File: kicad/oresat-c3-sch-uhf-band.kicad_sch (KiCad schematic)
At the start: 125 parts, among them Q3 NTR4101, Q4 PMV45EN, U16 AX5043, U18 LT5534, U19 BDCN-20-13+, U20 QPC1022, U21 TQP7M9105, U22 LT5534, U25 SN74LVC1G11IDCKRQ1, U26 TLV7041DBV, U27 LP2985AIM5-1.8_NOPB, U29 TQP3M9036, U32 SF2446E, U33 SF2446E, U40 MAX941EUA+, X1 TYKTBLSANF-16.000000

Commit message: Last of the ERC and DRC errors! only polishing left.
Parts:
- TP901, TP902, TP903, TP904, TP905, TP906, TP907, TP908, TP909: now left out of the parts list
- U40: footprint oresat-c3:21-0036K_MXM -> oresat-ics:LINEAR-MSOP-8-AND-MAXIM-UMAX-8-21-0036
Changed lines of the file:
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@@
   )
   (symbol (lib_id "oresat-misc:Test-Point-RF-Probe-Stripline") (at 281.94 101.6 180) (unit 1)
-    (in_bom yes) (on_board yes) (dnp no)
+    (in_bom no) (on_board yes) (dnp no)
     (property "Reference" "TP908" (at 281.94 99.06 0)
       (effects (font (size 1.27 1.0795)))
@@
   )
   (symbol (lib_id "oresat-misc:Test-Point-RF-Probe-Stripline") (at 203.2 226.06 180) (unit 1)
-    (in_bom yes) (on_board yes) (dnp no)
+    (in_bom no) (on_board yes) (dnp no)
     (property "Reference" "TP907" (at 203.2 223.52 0)
       (effects (font (size 1.27 1.0795)))
@@
       (effects (font (size 1.27 1.27)) (justify left))
     )
-    (property "Footprint" "oresat-c3:21-0036K_MXM" (at 62.23 18.415 0)
+    (property "Footprint" "oresat-ics:LINEAR-MSOP-8-AND-MAXIM-UMAX-8-21-0036" (at 62.23 18.415 0)
       (effects (font (size 1.27 1.27)) hide)
     )
@@
   )
   (symbol (lib_id "oresat-misc:Test-Point-RF-Probe-Stripline") (at 276.86 226.06 180) (unit 1)
-    (in_bom yes) (on_board yes) (dnp no)
+    (in_bom no) (on_board yes) (dnp no)
     (property "Reference" "TP906" (at 276.86 223.52 0)
       (effects (font (size 1.27 1.0795)))
@@
   )
   (symbol (lib_id "oresat-misc:Test-Point-RF-Probe-Stripline") (at 314.96 101.6 180) (unit 1)
-    (in_bom yes) (on_board yes) (dnp no)
+    (in_bom no) (on_board yes) (dnp no)
     (property "Reference" "TP905" (at 314.96 99.06 0)
       (effects (font (size 1.27 1.0795)))
@@
   )
   (symbol (lib_id "oresat-misc:Test-Point-RF-Probe-Stripline") (at 139.7 144.78 180) (unit 1)
-    (in_bom yes) (on_board yes) (dnp no)
+    (in_bom no) (on_board yes) (dnp no)
     (property "Reference" "TP901" (at 139.7 142.24 0)
       (effects (font (size 1.27 1.0795)))
@@
   )
   (symbol (lib_id "oresat-misc:Test-Point-RF-Probe-Stripline") (at 139.7 124.46 180) (unit 1)
-    (in_bom yes) (on_board yes) (dnp no)
+    (in_bom no) (on_board yes) (dnp no)
     (property "Reference" "TP902" (at 139.7 121.92 0)
       (effects (font (size 1.27 1.0795)))
@@
   )
   (symbol (lib_id "oresat-misc:Test-Point-RF-Probe-Stripline") (at 199.39 101.6 180) (unit 1)
-    (in_bom yes) (on_board yes) (dnp no)
+    (in_bom no) (on_board yes) (dnp no)
     (property "Reference" "TP909" (at 199.39 99.06 0)
       (effects (font (size 1.27 1.0795)))
@@
   )
   (symbol (lib_id "oresat-misc:Test-Point-RF-Probe-Stripline") (at 384.81 167.64 180) (unit 1)
-    (in_bom yes) (on_board yes) (dnp no)
+    (in_bom no) (on_board yes) (dnp no)
     (property "Reference" "TP903" (at 384.81 165.1 0)
       (effects (font (size 1.27 1.0795)))
@@
   )
   (symbol (lib_id "oresat-misc:Test-Point-RF-Probe-Stripline") (at 309.88 226.06 180) (unit 1)
-    (in_bom yes) (on_board yes) (dnp no)
+    (in_bom no) (on_board yes) (dnp no)
     (property "Reference" "TP904" (at 309.88 223.52 0)
       (effects (font (size 1.27 1.0795)))

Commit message: More polish; fixed all non-RF DRCs.
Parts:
- U21: footprint oresat-ics:U-QORVO-TQP7M9105-PA_TQP7M9105 -> oresat-ics:U-QORVO-TQP7M9105-VIAS
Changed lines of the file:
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@@
       (effects (font (size 1.27 1.27)))
     )
-    (property "Footprint" "oresat-ics:U-QORVO-TQP7M9105-PA_TQP7M9105" (at 227.33 93.98 0)
+    (property "Footprint" "oresat-ics:U-QORVO-TQP7M9105-VIAS" (at 227.33 93.98 0)
       (effects (font (size 1.27 1.27)) hide)
     )

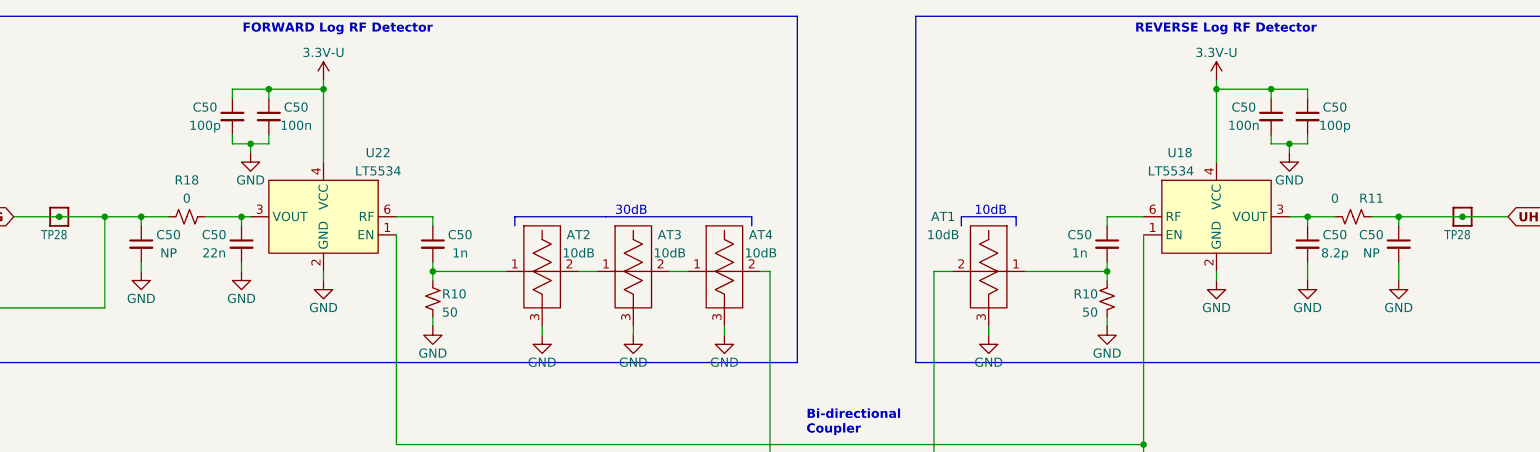
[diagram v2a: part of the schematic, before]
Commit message: More fixes. TOT_CLEAR moved to a non HH pin, cleaned up in2 zones, moved fiducials, set dv/dt on power switches, added HW ID (5 bits) rechecked ADC 1.8V limits and fixed resistor values to match.
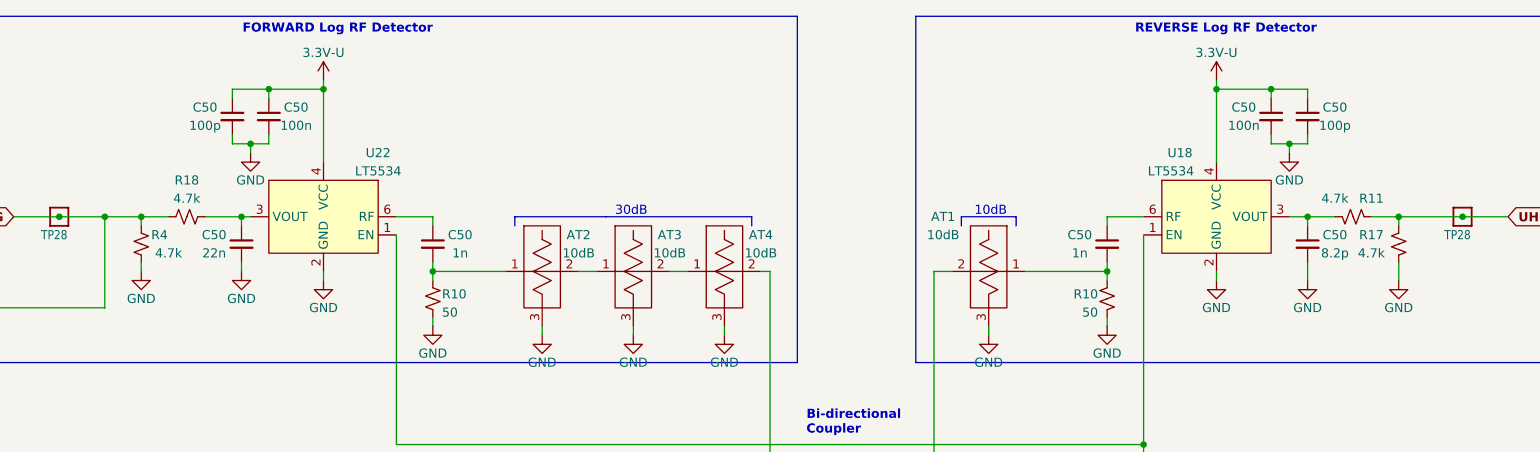
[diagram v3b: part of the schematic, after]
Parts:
- removed C50 (x2): NP, Capacitor_SMD:C_0603_1608Metric, symbol Device:C_Small
- added R17, R4: 4.7k, Resistor_SMD:R_0603_1608Metric, symbol Device:R_Small_US
- R11, R18: value 0 -> 4.7k
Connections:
- net GND: now also R17.2, R4.2
- net UHF_FWD_RF_LOG: now also R4.1
- net UHF_REV_RF_LOG: now also R17.1
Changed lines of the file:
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@@
       (effects (font (size 1.27 1.27)))
     )
-    (property "Value" "0" (at 367.03 50.8 90)
+    (property "Value" "4.7k" (at 367.03 50.8 90)
       (effects (font (size 1.27 1.27)))
     )
@@
     )
   )
-  (symbol (lib_id "Device:C_Small") (at 375.92 57.15 0) (mirror y) (unit 1)
-    (in_bom yes) (on_board yes) (dnp no)
-    (property "Reference" "C50" (at 372.11 55.88 0)
-      (effects (font (size 1.27 1.27)))
-    )
-    (property "Value" "NP" (at 372.11 58.42 0)
-      (effects (font (size 1.27 1.27)))
-    )
-    (property "Footprint" "Capacitor_SMD:C_0603_1608Metric" (at 375.92 57.15 0)
-      (effects (font (size 1.27 1.27)) hide)
-    )
-    (property "Datasheet" "~" (at 375.92 57.15 0)
-      (effects (font (size 1.27 1.27)) hide)
-    )
-    (pin "1")
-    (pin "2")
-    (instances
-      (project "oresat-c3"
-        (path "/65d12cdd-c326-4033-9053-c59fa4e0b25e/1b68ea4b-cacf-4529-b1d4-9be5d7c1043c"
-          (reference "C50") (unit 1)
-        )
-        (path "/65d12cdd-c326-4033-9053-c59fa4e0b25e/05e45903-5042-4bc1-87af-e9d7510ea02d"
-          (reference "C56") (unit 1)
-        )
-      )
-    )
-  )
   (symbol (lib_id "Device:L_Small") (at 264.16 101.6 270) (mirror x) (unit 1)
     (in_bom yes) (on_board yes) (dnp no)
@@
     )
   )
+  (symbol (lib_id "Device:R_Small_US") (at 375.92 57.15 0) (mirror y) (unit 1)
+    (in_bom yes) (on_board yes) (dnp no)
+    (property "Reference" "R17" (at 372.11 55.88 0)
+      (effects (font (size 1.27 1.27)))
+    )
+    (property "Value" "4.7k" (at 372.11 58.42 0)
+      (effects (font (size 1.27 1.27)))
+    )
+    (property "Footprint" "Resistor_SMD:R_0603_1608Metric" (at 375.92 57.15 0)
+      (effects (font (size 1.27 1.27)) hide)
+    )
+    (property "Datasheet" "~" (at 375.92 57.15 0)
+      (effects (font (size 1.27 1.27)) hide)
+    )
+    (pin "1")
+    (pin "2")
+    (instances
+      (project "oresat-c3"
+        (path "/65d12cdd-c326-4033-9053-c59fa4e0b25e/05e45903-5042-4bc1-87af-e9d7510ea02d"
+          (reference "R17") (unit 1)
+        )
+      )
+    )
+  )
   (symbol (lib_id "Device:C_Small") (at 217.17 213.36 0) (mirror y) (unit 1)
     (in_bom yes) (on_board yes) (dnp no)
@@
     )
   )
+  (symbol (lib_id "Device:R_Small_US") (at 200.66 57.15 0) (unit 1)
+    (in_bom yes) (on_board yes) (dnp no)
+    (property "Reference" "R4" (at 203.2 55.88 0)
+      (effects (font (size 1.27 1.27)))
+    )
+    (property "Value" "4.7k" (at 204.47 58.42 0)
+      (effects (font (size 1.27 1.27)))
+    )
+    (property "Footprint" "Resistor_SMD:R_0603_1608Metric" (at 200.66 57.15 0)
+      (effects (font (size 1.27 1.27)) hide)
+    )
+    (property "Datasheet" "~" (at 200.66 57.15 0)
+      (effects (font (size 1.27 1.27)) hide)
+    )
+    (pin "1")
+    (pin "2")
+    (instances
+      (project "oresat-c3"
+        (path "/65d12cdd-c326-4033-9053-c59fa4e0b25e/05e45903-5042-4bc1-87af-e9d7510ea02d"
+          (reference "R4") (unit 1)
+        )
+      )
+    )
+  )
   (symbol (lib_id "Device:L_Small") (at 101.6 114.3 0) (mirror y) (unit 1)
     (in_bom yes) (on_board yes) (dnp no)
@@
     )
   )
-  (symbol (lib_id "Device:C_Small") (at 200.66 57.15 0) (unit 1)
-    (in_bom yes) (on_board yes) (dnp no)
-    (property "Reference" "C50" (at 204.47 55.88 0)
-      (effects (font (size 1.27 1.27)))
-    )
-    (property "Value" "NP" (at 204.47 58.42 0)
-      (effects (font (size 1.27 1.27)))
-    )
-    (property "Footprint" "Capacitor_SMD:C_0603_1608Metric" (at 200.66 57.15 0)
-      (effects (font (size 1.27 1.27)) hide)
-    )
-    (property "Datasheet" "~" (at 200.66 57.15 0)
-      (effects (font (size 1.27 1.27)) hide)
-    )
-    (pin "1")
-    (pin "2")
-    (instances
-      (project "oresat-c3"
-        (path "/65d12cdd-c326-4033-9053-c59fa4e0b25e/1b68ea4b-cacf-4529-b1d4-9be5d7c1043c"
-          (reference "C50") (unit 1)
-        )
-        (path "/65d12cdd-c326-4033-9053-c59fa4e0b25e/05e45903-5042-4bc1-87af-e9d7510ea02d"
-          (reference "C65") (unit 1)
-        )
-      )
-    )
-  )
   (symbol (lib_id "Device:C_Small") (at 241.3 57.15 0) (unit 1)
     (in_bom yes) (on_board yes) (dnp no)
@@
       (effects (font (size 1.27 1.27)))
     )
-    (property "Value" "0" (at 207.01 50.8 90)
+    (property "Value" "4.7k" (at 207.01 50.8 90)
       (effects (font (size 1.27 1.27)))
     )
